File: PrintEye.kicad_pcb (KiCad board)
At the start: 2 copper layers, 52.1 x 29.8 mm, 18 parts, among them J1 FTDI, J2 Pause Button, J3 Activity LED, Q1 2N7000, Q2 2N7000, U1 ATmega328-PU, Y1 16MHz

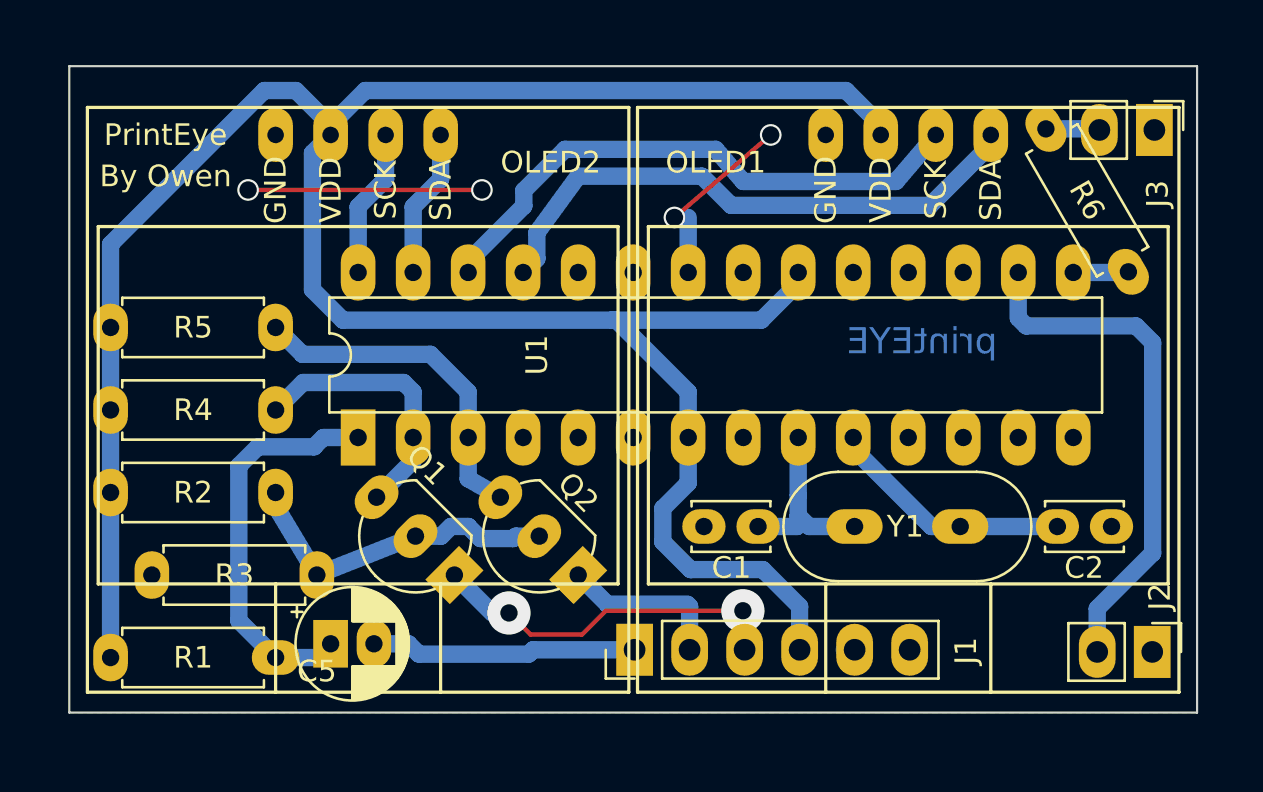
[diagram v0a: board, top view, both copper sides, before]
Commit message: Track widths and clearances
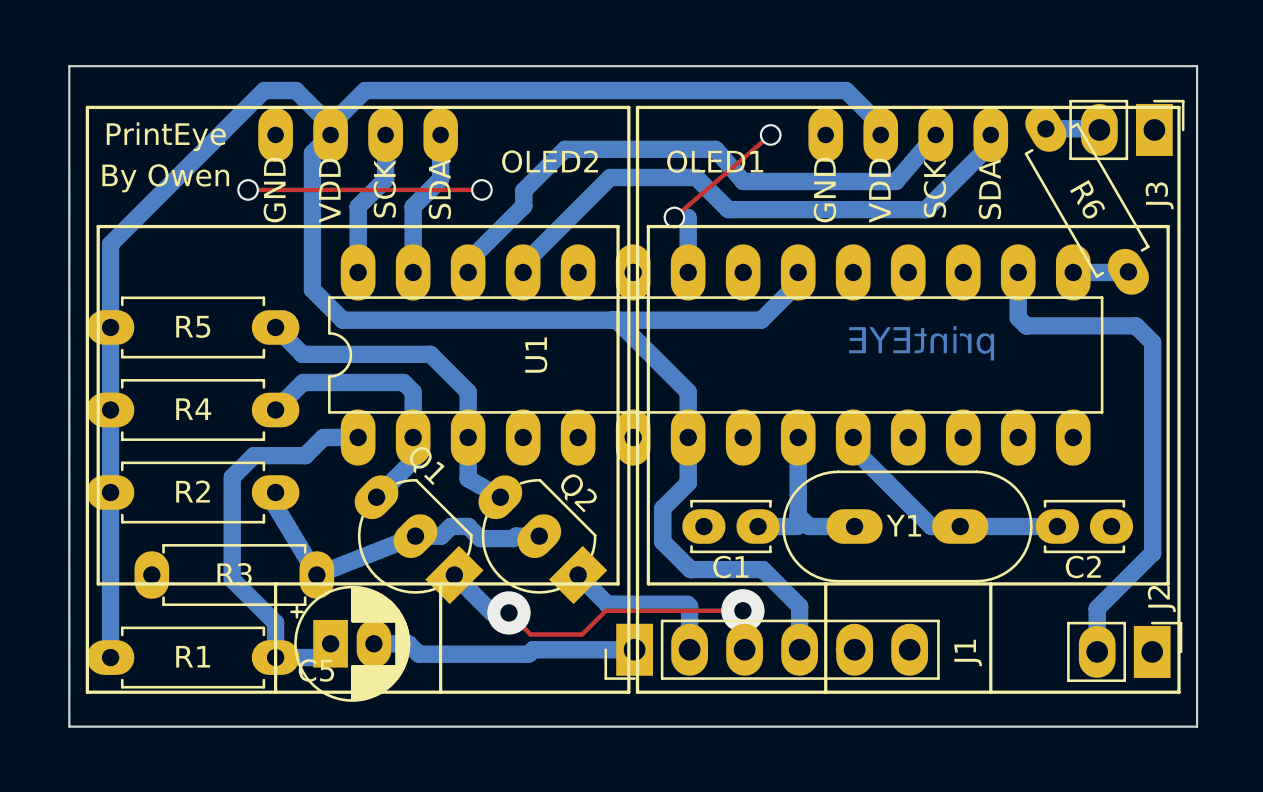
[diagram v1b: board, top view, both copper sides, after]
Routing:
- net SDA1: track 27.0 -> 25.9 mm
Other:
- board size 52.1 x 29.8 mm -> 52.1 x 30.5 mm
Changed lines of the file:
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@@
     (thickness 1.6)
     (drawings 7)
-    (tracks 136)
+    (tracks 135)
     (zones 0)
     (modules 18)
@@
   (page A4)
   (layers
-    (0 F.Cu signal hide)
+    (0 F.Cu signal)
     (31 B.Cu signal)
     (37 F.SilkS user)
@@
     (mod_text_size 1 1)
     (mod_text_width 0.15)
-    (pad_size 2.4 1.7)
-    (pad_drill 1)
+    (pad_size 2.6 1.6)
+    (pad_drill 0.8)
     (pad_to_mask_clearance 0.051)
     (solder_mask_min_width 0.25)
-    (aux_axis_origin 120.015 118.11)
-    (grid_origin 120.015 118.11)
+    (aux_axis_origin 120.015 118.76)
+    (grid_origin 120.015 118.76)
     (visible_elements FFFFFF7F)
     (pcbplotparams
@@
     (fp_line (start 0.66 1.25) (end 6.96 1.25) (layer F.Fab) (width 0.1))
     (fp_line (start 0.66 -1.25) (end 0.66 1.25) (layer F.Fab) (width 0.1))
-    (pad 2 thru_hole oval (at 7.62 0) (size 1.6 2.2) (drill 0.8) (layers *.Cu *.Mask)
+    (pad 2 thru_hole oval (at 7.62 0) (size 2.2 1.6) (drill 0.8) (layers *.Cu *.Mask)
       (net 6 TX))
-    (pad 1 thru_hole oval (at 0 0) (size 1.6 2.2) (drill 0.8) (layers *.Cu *.Mask)
+    (pad 1 thru_hole oval (at 0 0) (size 2.2 1.6) (drill 0.8) (layers *.Cu *.Mask)
       (net 4 5v))
     (model ${KISYS3DMOD}/Resistor_THT.3dshapes/R_Axial_DIN0207_L6.3mm_D2.5mm_P7.62mm_Horizontal.wrl
@@
     (fp_line (start 0.66 1.25) (end 6.96 1.25) (layer F.Fab) (width 0.1))
     (fp_line (start 0.66 -1.25) (end 0.66 1.25) (layer F.Fab) (width 0.1))
-    (pad 2 thru_hole oval (at 7.62 0) (size 1.6 2.2) (drill 0.8) (layers *.Cu *.Mask)
+    (pad 2 thru_hole oval (at 7.62 0) (size 2.2 1.6) (drill 0.8) (layers *.Cu *.Mask)
       (net 7 RX))
-    (pad 1 thru_hole oval (at 0 0) (size 1.6 2.2) (drill 0.8) (layers *.Cu *.Mask)
+    (pad 1 thru_hole oval (at 0 0) (size 2.2 1.6) (drill 0.8) (layers *.Cu *.Mask)
       (net 4 5v))
     (model ${KISYS3DMOD}/Resistor_THT.3dshapes/R_Axial_DIN0207_L6.3mm_D2.5mm_P7.62mm_Horizontal.wrl
@@
     (fp_line (start 0.66 1.25) (end 6.96 1.25) (layer F.Fab) (width 0.1))
     (fp_line (start 0.66 -1.25) (end 0.66 1.25) (layer F.Fab) (width 0.1))
-    (pad 2 thru_hole oval (at 7.62 0) (size 1.6 2.2) (drill 0.8) (layers *.Cu *.Mask)
+    (pad 2 thru_hole oval (at 7.62 0) (size 2.2 1.6) (drill 0.8) (layers *.Cu *.Mask)
       (net 5 3v3))
-    (pad 1 thru_hole oval (at 0 0) (size 1.6 2.2) (drill 0.8) (layers *.Cu *.Mask)
+    (pad 1 thru_hole oval (at 0 0) (size 2.2 1.6) (drill 0.8) (layers *.Cu *.Mask)
       (net 4 5v))
     (model ${KISYS3DMOD}/Resistor_THT.3dshapes/R_Axial_DIN0207_L6.3mm_D2.5mm_P7.62mm_Horizontal.wrl
@@
     (fp_line (start 0.66 1.25) (end 6.96 1.25) (layer F.Fab) (width 0.1))
     (fp_line (start 0.66 -1.25) (end 0.66 1.25) (layer F.Fab) (width 0.1))
-    (pad 2 thru_hole oval (at 7.62 0 180) (size 1.6 2.2) (drill 0.8) (layers *.Cu *.Mask)
+    (pad 2 thru_hole oval (at 7.62 0 180) (size 2.2 1.6) (drill 0.8) (layers *.Cu *.Mask)
       (net 4 5v))
     (pad 1 thru_hole oval (at 0 0 270) (size 1.6 2.2) (drill 0.8) (layers *.Cu *.Mask)
@@
     (pad 15 thru_hole oval (at 7.62 33.02 90) (size 2.6 1.6) (drill 0.8) (layers *.Cu *.Mask)
       (net 16 "Net-(R6-Pad1)"))
-    (pad 1 thru_hole rect (at 0 0 90) (size 2.6 1.6) (drill 0.8) (layers *.Cu *.Mask)
+    (pad 1 thru_hole oval (at 0 0 90) (size 2.6 1.6) (drill 0.8) (layers *.Cu *.Mask)
       (net 11 "Net-(C5-Pad1)"))
     (model ${KISYS3DMOD}/Package_DIP.3dshapes/DIP-28_W7.62mm.wrl
@@
     )
   )
-  (gr_line (start 120.015 118.11) (end 120.015 88.265) (layer Edge.Cuts) (width 0.1))
-  (gr_line (start 172.085 118.11) (end 120.015 118.11) (layer Edge.Cuts) (width 0.1))
-  (gr_line (start 172.085 88.265) (end 172.085 118.11) (layer Edge.Cuts) (width 0.1))
+  (gr_line (start 120.015 118.76) (end 120.015 88.265) (layer Edge.Cuts) (width 0.1))
+  (gr_line (start 172.085 118.76) (end 120.015 118.76) (layer Edge.Cuts) (width 0.1))
+  (gr_line (start 172.085 88.265) (end 172.085 118.76) (layer Edge.Cuts) (width 0.1))
   (gr_line (start 120.015 88.265) (end 172.085 88.265) (layer Edge.Cuts) (width 0.1))
   (gr_text printEYE (at 159.385 100.965) (layer B.Cu)
@@
   (segment (start 141.427002 115.21) (end 141.227001 115.410001) (width 0.8) (layer B.Cu) (net 8))
   (segment (start 146.115 115.21) (end 141.427002 115.21) (width 0.8) (layer B.Cu) (net 8))
-  (segment (start 140.97 97.29) (end 140.97 97.79) (width 0.8) (layer B.Cu) (net 9))
-  (segment (start 141.605 95.95349) (end 141.605 97.155) (width 0.8) (layer B.Cu) (net 9))
-  (segment (start 143.51 93.345) (end 141.605 95.95349) (width 0.8) (layer B.Cu) (net 9))
-  (segment (start 141.605 97.155) (end 140.97 97.79) (width 0.8) (layer B.Cu) (net 9))
-  (segment (start 149.225 93.345) (end 143.51 93.345) (width 0.8) (layer B.Cu) (net 9))
   (segment (start 162.56 91.89) (end 162.56 91.44) (width 0.8) (layer B.Cu) (net 9))
-  (segment (start 159.75998 94.69002) (end 162.56 91.89) (width 0.8) (layer B.Cu) (net 9))
-  (segment (start 150.57002 94.69002) (end 159.75998 94.69002) (width 0.8) (layer B.Cu) (net 9))
-  (segment (start 149.225 93.345) (end 150.57002 94.69002) (width 0.8) (layer B.Cu) (net 9))
+  (segment (start 159.55998 94.89002) (end 162.56 91.89) (width 0.8) (layer B.Cu) (net 9))
+  (segment (start 144.990812 93.405011) (end 148.960011 93.405011) (width 0.8) (layer B.Cu) (net 9))
+  (segment (start 150.44502 94.89002) (end 159.55998 94.89002) (width 0.8) (layer B.Cu) (net 9))
+  (segment (start 148.960011 93.405011) (end 150.44502 94.89002) (width 0.8) (layer B.Cu) (net 9))
+  (segment (start 140.97 97.425823) (end 144.990812 93.405011) (width 0.8) (layer B.Cu) (net 9))
+  (segment (start 140.97 97.79) (end 140.97 97.425823) (width 0.8) (layer B.Cu) (net 9))
   (segment (start 135.89 94.76) (end 135.89 95.69) (width 0.8) (layer B.Cu) (net 10))
   (segment (start 137.16 93.49) (end 135.89 94.76) (width 0.8) (layer B.Cu) (net 10))
   (segment (start 135.89 95.69) (end 135.89 97.79) (width 0.8) (layer B.Cu) (net 10))
   (segment (start 137.16 91.44) (end 137.16 93.49) (width 0.8) (layer B.Cu) (net 10))
-  (segment (start 131.319999 105.840001) (end 131.75 105.41) (width 0.8) (layer B.Cu) (net 11))
-  (segment (start 128.723999 105.840001) (end 131.319999 105.840001) (width 0.8) (layer B.Cu) (net 11))
-  (segment (start 131.75 105.41) (end 133.35 105.41) (width 0.8) (layer B.Cu) (net 11))
-  (segment (start 127.839999 106.724001) (end 128.723999 105.840001) (width 0.8) (layer B.Cu) (net 11))
-  (segment (start 127.839999 113.869999) (end 127.839999 106.724001) (width 0.8) (layer B.Cu) (net 11))
-  (segment (start 129.54 115.57) (end 127.839999 113.869999) (width 0.8) (layer B.Cu) (net 11))
+  (segment (start 127.53999 111.96999) (end 129.54 113.97) (width 0.8) (layer B.Cu) (net 11))
+  (segment (start 129.54 113.97) (end 129.54 115.57) (width 0.8) (layer B.Cu) (net 11))
+  (segment (start 127.53999 107.245833) (end 127.53999 111.96999) (width 0.8) (layer B.Cu) (net 11))
+  (segment (start 128.535833 106.24999) (end 127.53999 107.245833) (width 0.8) (layer B.Cu) (net 11))
+  (segment (start 130.91001 106.24999) (end 128.535833 106.24999) (width 0.8) (layer B.Cu) (net 11))
+  (segment (start 131.75 105.41) (end 130.91001 106.24999) (width 0.8) (layer B.Cu) (net 11))
+  (segment (start 133.35 105.41) (end 131.75 105.41) (width 0.8) (layer B.Cu) (net 11))
   (segment (start 131.445 115.57) (end 132.08 114.935) (width 0.8) (layer B.Cu) (net 11))
   (segment (start 129.54 115.57) (end 131.445 115.57) (width 0.8) (layer B.Cu) (net 11))
@@
   (via (at 151.115 113.41) (size 2) (drill 0.8) (layers F.Cu B.Cu) (net 13))
   (segment (start 139.545 113.51) (end 137.795 111.76) (width 0.8) (layer B.Cu) (net 13))
-  (segment (start 151.115 115.13) (end 151.195 115.21) (width 0.8) (layer B.Cu) (net 13))
-  (segment (start 151.115 113.41) (end 151.115 115.13) (width 0.8) (layer B.Cu) (net 13))
   (segment (start 141.314999 114.509999) (end 140.315 113.51) (width 0.2) (layer F.Cu) (net 13))
   (segment (start 143.684999 114.509999) (end 141.314999 114.509999) (width 0.2) (layer F.Cu) (net 13))
   (segment (start 144.784998 113.41) (end 143.684999 114.509999) (width 0.2) (layer F.Cu) (net 13))
   (segment (start 151.115 113.41) (end 144.784998 113.41) (width 0.2) (layer F.Cu) (net 13))
+  (segment (start 151.115 115.13) (end 151.195 115.21) (width 0.8) (layer B.Cu) (net 13))
+  (segment (start 151.115 113.41) (end 151.115 115.13) (width 0.8) (layer B.Cu) (net 13))
   (segment (start 163.83 99.89) (end 164.2 100.26) (width 0.8) (layer B.Cu) (net 14))
   (segment (start 163.83 97.79) (end 163.83 99.89) (width 0.8) (layer B.Cu) (net 14))
@@
     (polygon
       (pts
-        (xy 120.015 118.11) (xy 120.015 88.265) (xy 172.085 88.265) (xy 172.085 118.11)
+        (xy 120.03 118.76) (xy 120.015 88.265) (xy 172.085 88.265) (xy 172.1 118.76)
       )
     )

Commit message: Capacitor ended up joined on PCB, trivial correction to it's pads
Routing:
- net SDA1: track 25.9 -> 28.1 mm
- net 5v: track 115.1 -> 116.2 mm
- net 3v3: track 15.4 -> 16.4 mm
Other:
- board size 52.1 x 30.5 mm -> 52.1 x 30.6 mm
- board text added: "OPC"
- board text removed: "printEYE"

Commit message: Update with final schematic and pcb revs
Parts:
- C5: footprint Capacitor_THT:CP_Radial_D5.0mm_P2.00mm -> Capacitor_THT:C_Disc_D3.8mm_W2.6mm_P2.50mm
- J1, J2: moved to B.Cu
- turned J1 to 270 degrees
- turned J2 to 90 degrees
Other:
- board text removed: "OPC"
